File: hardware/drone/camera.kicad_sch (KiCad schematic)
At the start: 1 part, among them U1 STM32N645I0

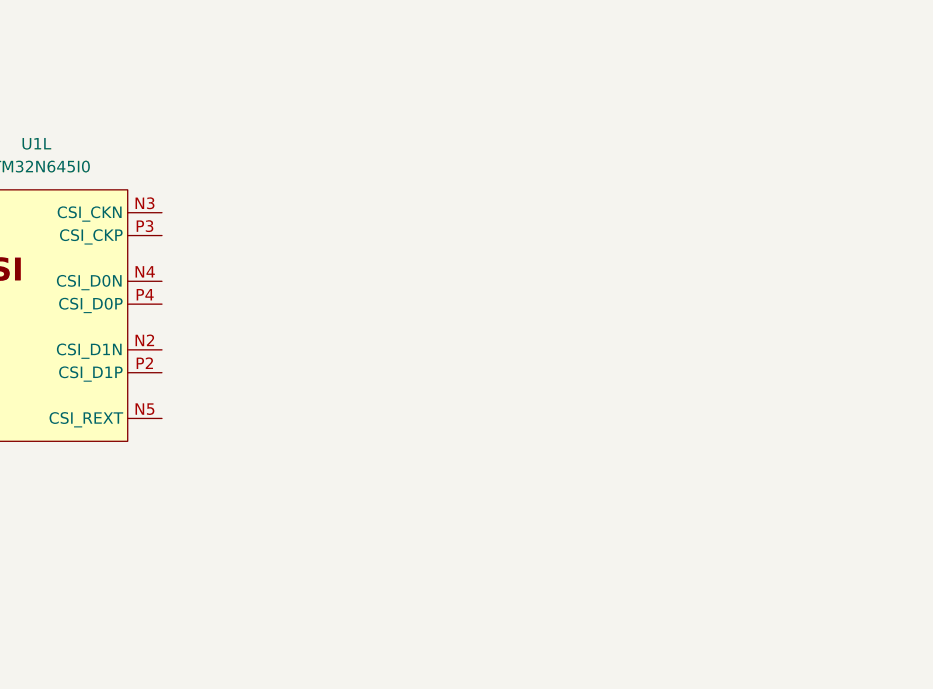
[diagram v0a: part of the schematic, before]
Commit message: Continued PDN and started camera schematic
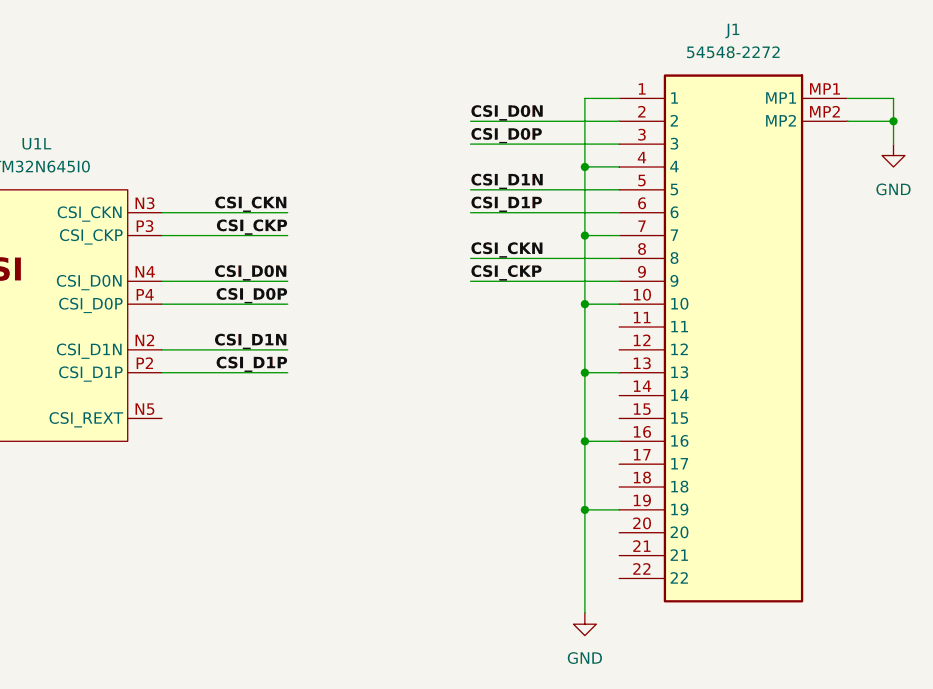
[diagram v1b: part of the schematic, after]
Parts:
- added J1: 54548-2272, 545482272, symbol 54548-2272:54548-2272
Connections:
- net CSI_D1N: now reaches U1.N2 (CSI_D1N)
- net CSI_D1N: now also J1.5
- net CSI_CKN: now reaches U1.N3 (CSI_CKN)
- net CSI_CKN: now also J1.8
- net CSI_D0N: now reaches U1.N4 (CSI_D0N)
- net CSI_D0N: now also J1.2
- net CSI_D1P: now reaches U1.P2 (CSI_D1P)
- net CSI_D1P: now also J1.6
- net CSI_CKP: now reaches U1.P3 (CSI_CKP)
- net CSI_CKP: now also J1.9
- net CSI_D0P: now reaches U1.P4 (CSI_D0P)
- net CSI_D0P: now also J1.3
- new net GND: J1.1, J1.10, J1.13, J1.16, J1.19, J1.4, J1.7, J1.MP1, J1.MP2

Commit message: cleanup
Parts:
- J1: footprint 545482272 -> 54548-2272:545482272
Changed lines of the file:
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@@
 			)
 		)
-		(property "Footprint" "545482272"
+		(property "Footprint" "54548-2272:545482272"
 			(at 140.97 139.37 0)
 			(hide yes)

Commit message: More work on power architecture
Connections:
- no-connect marks 0 -> 4
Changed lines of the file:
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@@
 		(color 0 0 0 0)
+	)
+	(no_connect
+		(at 137.16 77.47)
+	)
+	(no_connect
+		(at 137.16 72.39)
+	)
+	(no_connect
+		(at 137.16 80.01)
+	)
+	(no_connect
+		(at 137.16 69.85)
 	)
 	(wire

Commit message: more radio work
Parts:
- U1: footprint STM32N645I0:BGA178C80P14X14_1200X1200X100 -> (none)

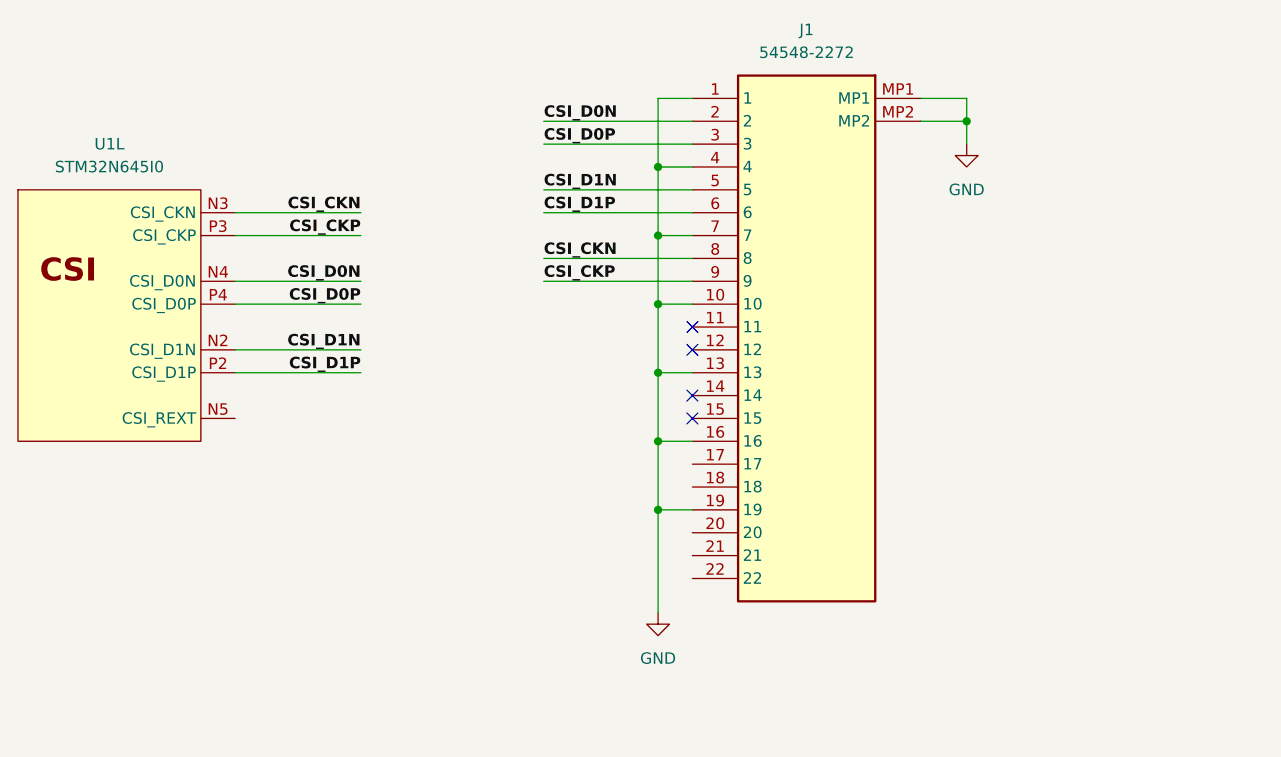
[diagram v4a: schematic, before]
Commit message: Finished MCU schematic decoupling, finished system control schematic
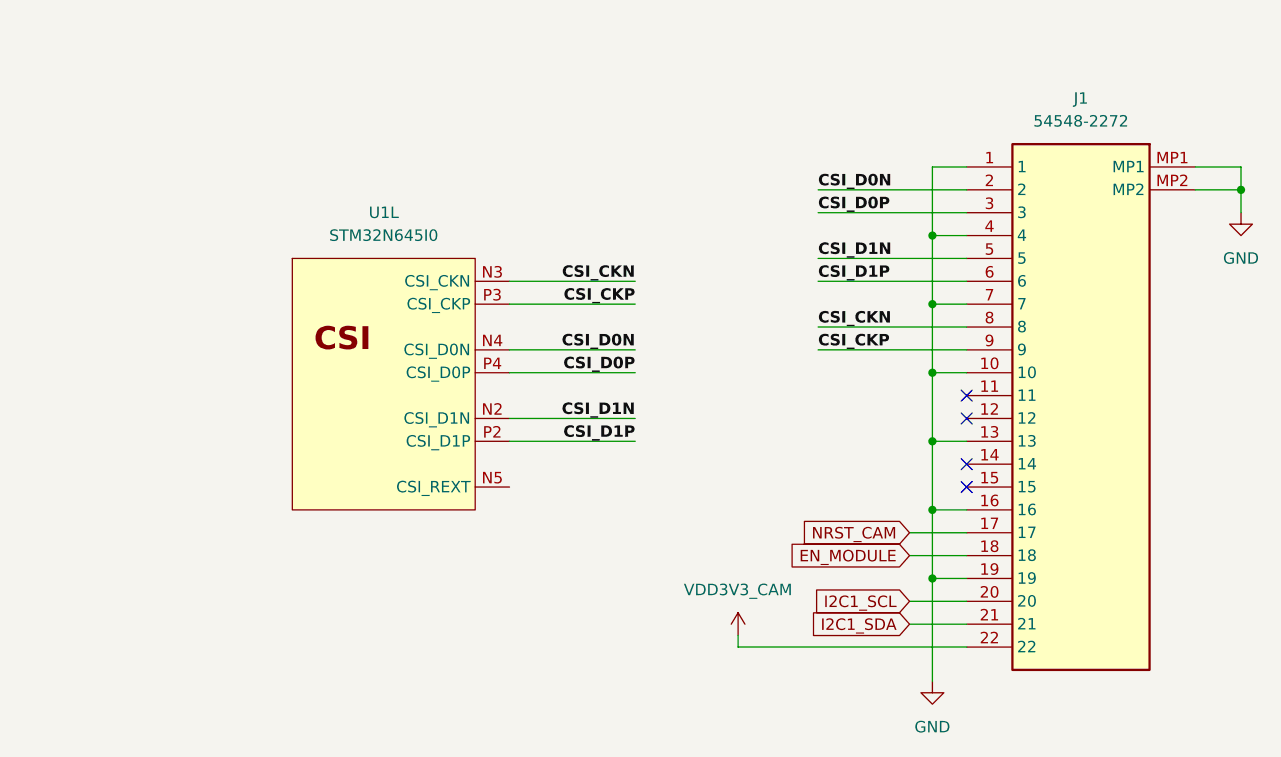
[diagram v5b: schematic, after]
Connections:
- net NRST_CAM: now reaches J1.17
- net EN_MODULE: now reaches J1.18
- net I2C1_SCL: now reaches J1.20
- net I2C1_SDA: now reaches J1.21
- net VDD3V3_CAM: now reaches J1.22
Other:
- moved on the sheet: J1, U1L

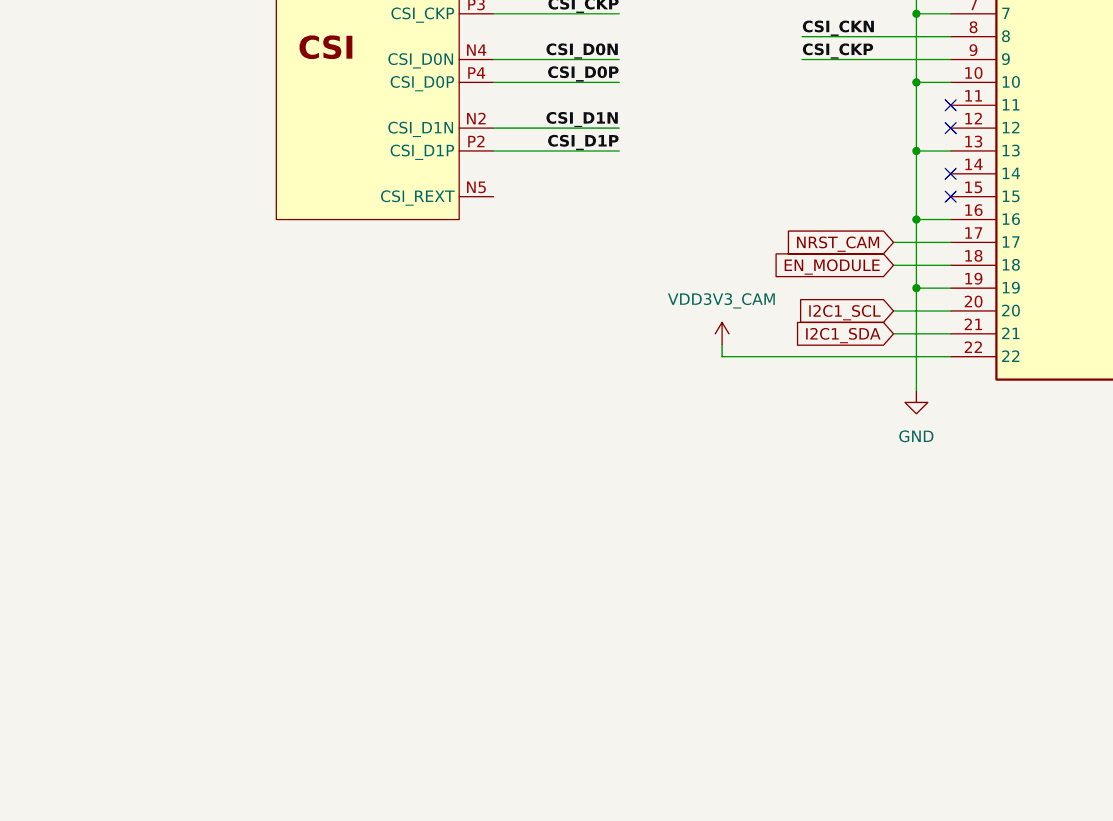
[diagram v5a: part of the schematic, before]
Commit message: Created pinmux table and completed pinmuxing
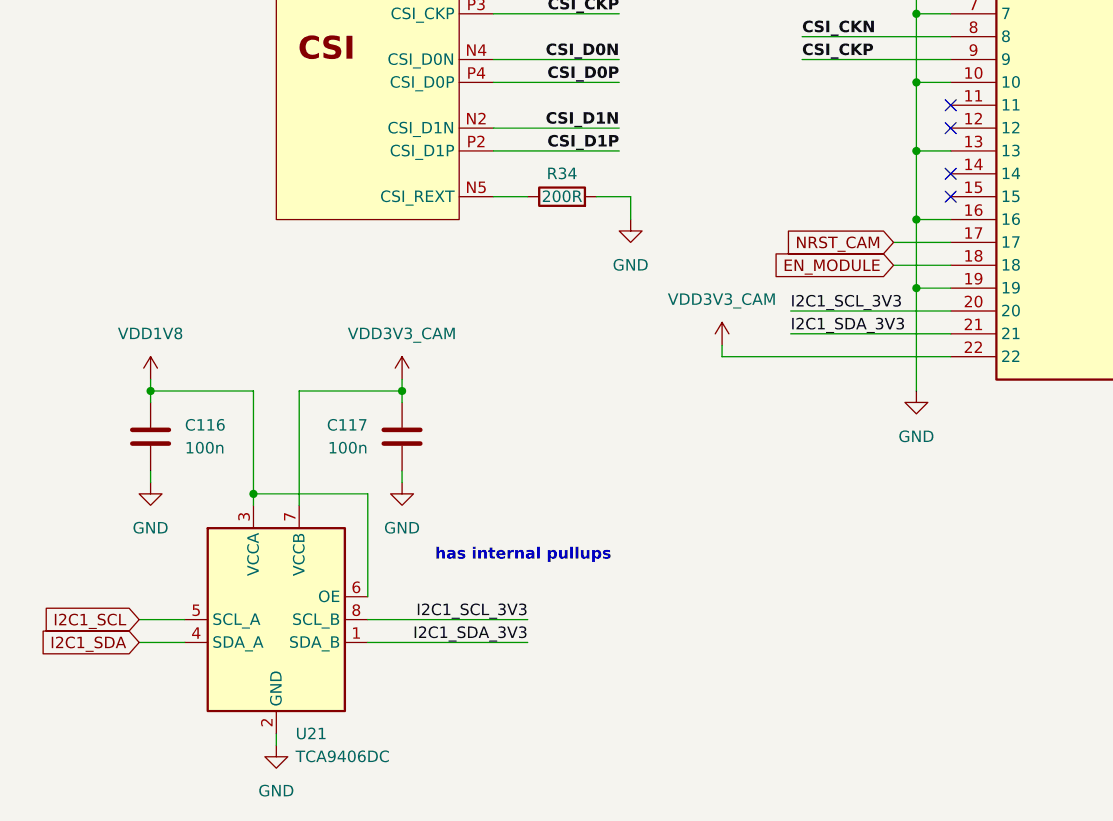
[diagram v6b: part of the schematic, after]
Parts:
- added C116, C117: 100n, symbol Device:C
- added R34: 200R, symbol Device:R
- added U21: TCA9406DC, symbol Interface:TCA9406DC
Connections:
- net GND: now also C116.2, C117.2, R34.2, U21.2 (GND)
- net I2C1_SCL: now also U21.5 (SCL_A); no longer J1.20
- net I2C1_SDA: now also U21.4 (SDA_A); no longer J1.21
- net VDD3V3_CAM: now also C117.1, U21.7 (VCCB)
- net at U1.N5 (CSI_REXT): now also R34.1
- new net I2C1_SCL_3V3: J1.20, U21.8 (SCL_B)
- new net I2C1_SDA_3V3: J1.21, U21.1 (SDA_B)
- new net VDD1V8: C116.1, U21.3 (VCCA), U21.6 (OE)
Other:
- note added: "has internal pullups"

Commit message: Small cleanup
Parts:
- U1: footprint (none) -> STM32N645I0:BGA178C80P14X14_1200X1200X100
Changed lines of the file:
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@@
 			)
 		)
-		(property "Footprint" ""
+		(property "Footprint" "STM32N645I0:BGA178C80P14X14_1200X1200X100"
 			(at 102.87 76.2 0)
 			(hide yes)

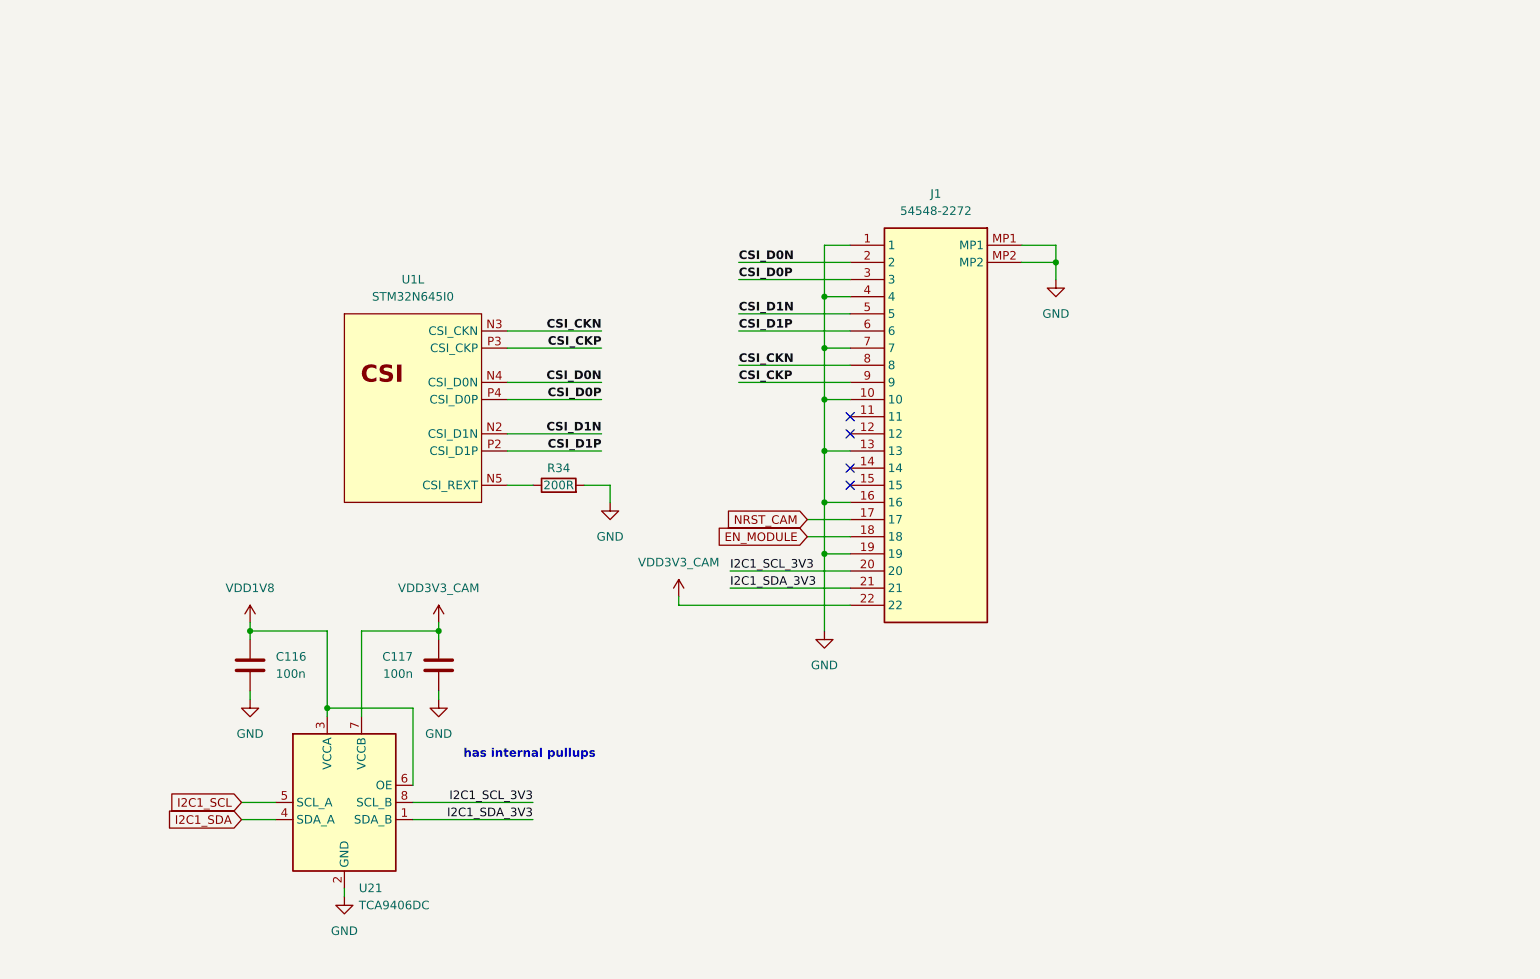
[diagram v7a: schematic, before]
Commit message: Fixed some pullups and pinmuxxed more
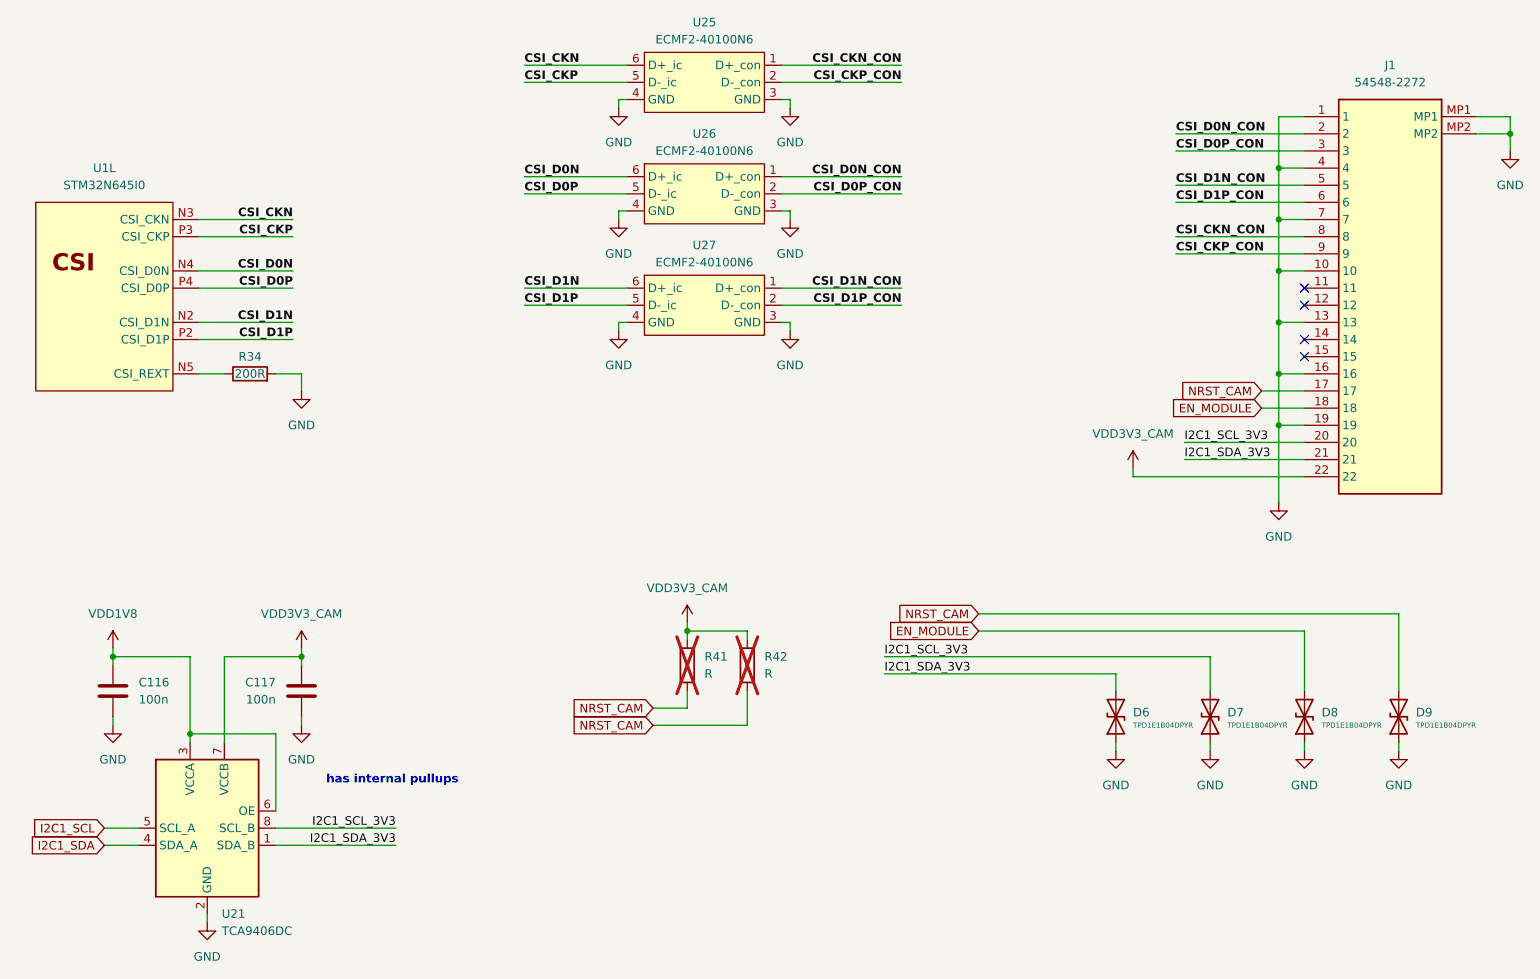
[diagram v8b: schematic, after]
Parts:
- added D6, D7, D8, D9: TPD1E1B04DPYR, Package_DIP:DIP-40_W15.24mm, symbol Device:D_TVS
- added R41, R42: R, symbol Device:R
- added U25, U26, U27: ECMF2-40100N6, Package_DFN_QFN:ST_UQFN-6L_1.5x1.7mm_P0.5mm, symbol SoftDrone:ECMF2-40100N6
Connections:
- net CSI_CKN: now also U25.6 (D+_ic); no longer J1.8
- net CSI_CKP: now also U25.5 (D-_ic); no longer J1.9
- net CSI_D0N: now also U26.6 (D+_ic); no longer J1.2
- net CSI_D0P: now also U26.5 (D-_ic); no longer J1.3
- net CSI_D1N: now also U27.6 (D+_ic); no longer J1.5
- net CSI_D1P: now also U27.5 (D-_ic); no longer J1.6
- net EN_MODULE: now also D8.2 (A2)
- net GND: now also D6.1 (A1), D7.1 (A1), D8.1 (A1), D9.1 (A1), U25.3 (GND), U25.4 (GND), U26.3 (GND), U26.4 (GND), U27.3 (GND), U27.4 (GND)
- net I2C1_SCL_3V3: now also D7.2 (A2)
- net I2C1_SDA_3V3: now also D6.2 (A2)
- net NRST_CAM: now also D9.2 (A2), R41.2, R42.2
- net VDD3V3_CAM: now also R41.1, R42.1
- new net CSI_CKN_CON: J1.8, U25.1 (D+_con)
- new net CSI_CKP_CON: J1.9, U25.2 (D-_con)
- new net CSI_D0N_CON: J1.2, U26.1 (D+_con)
- new net CSI_D0P_CON: J1.3, U26.2 (D-_con)
- new net CSI_D1N_CON: J1.5, U27.1 (D+_con)
- new net CSI_D1P_CON: J1.6, U27.2 (D-_con)
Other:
- moved on the sheet: C116, C117, J1, R34, U1L, U21
